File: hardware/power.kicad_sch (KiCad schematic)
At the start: 15 parts, among them J4 Conn_Coaxial_Small, J5 batt, Q1 PMOS, Q2 PMOS, SW41 SW_SPDT, U4 TLV62569DBV

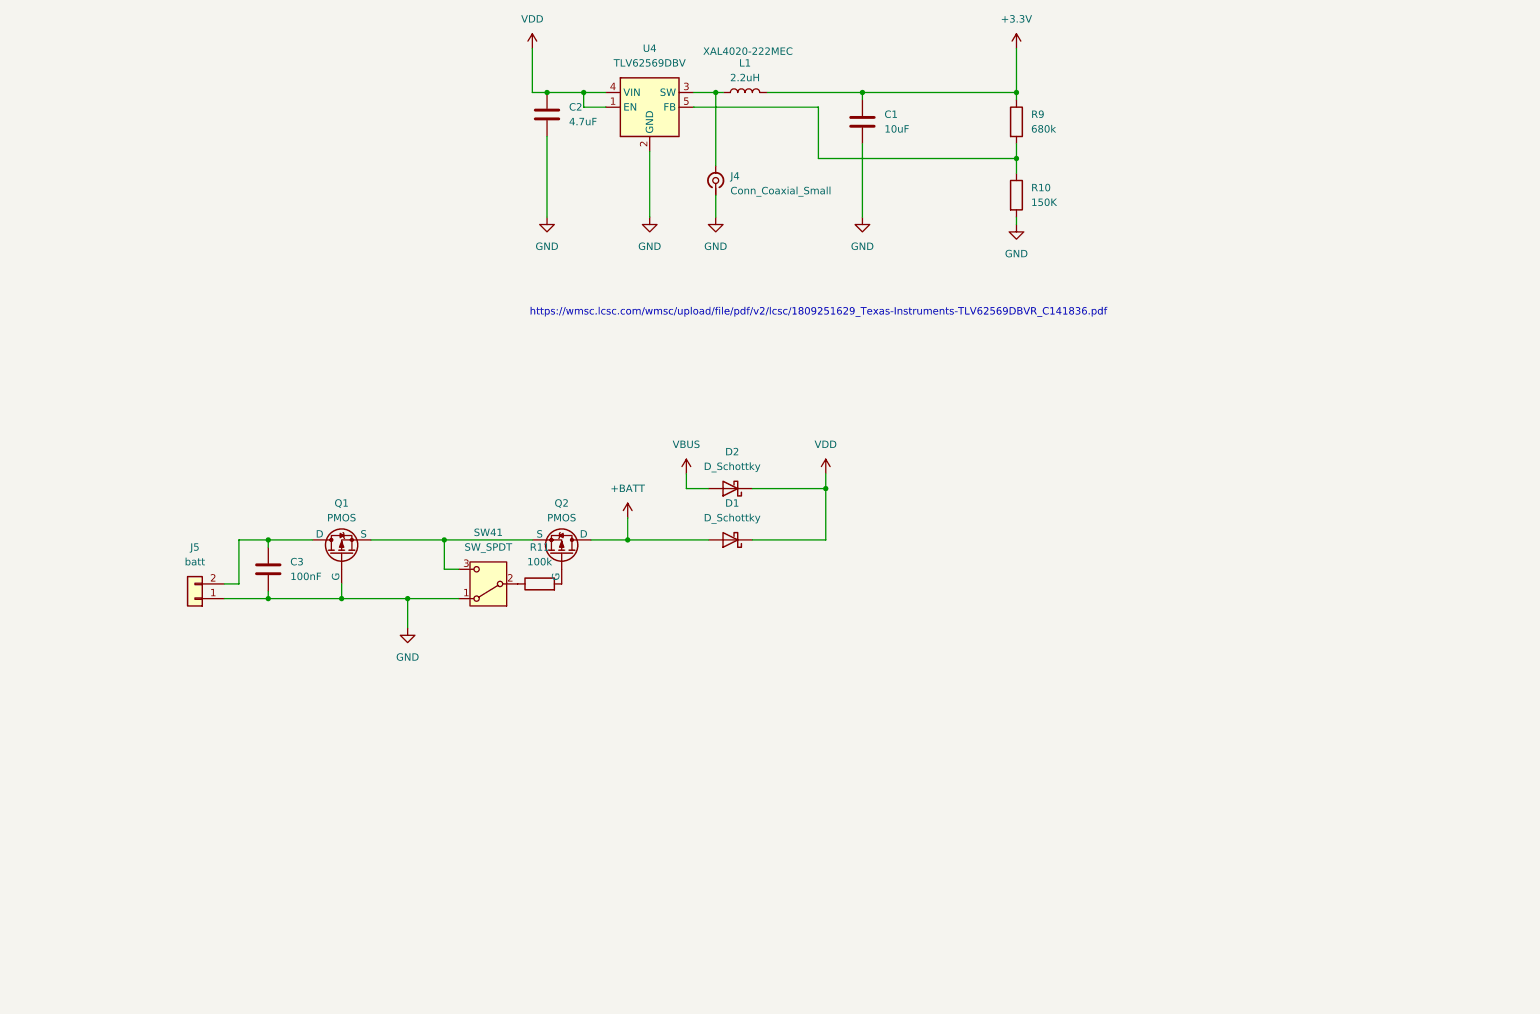
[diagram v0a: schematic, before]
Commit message: Add the battery charger
This commit will remove the old battery switching logic, and replace it
with a BQ24075.
Some more info are required, so the component that need a value are marked as TBD
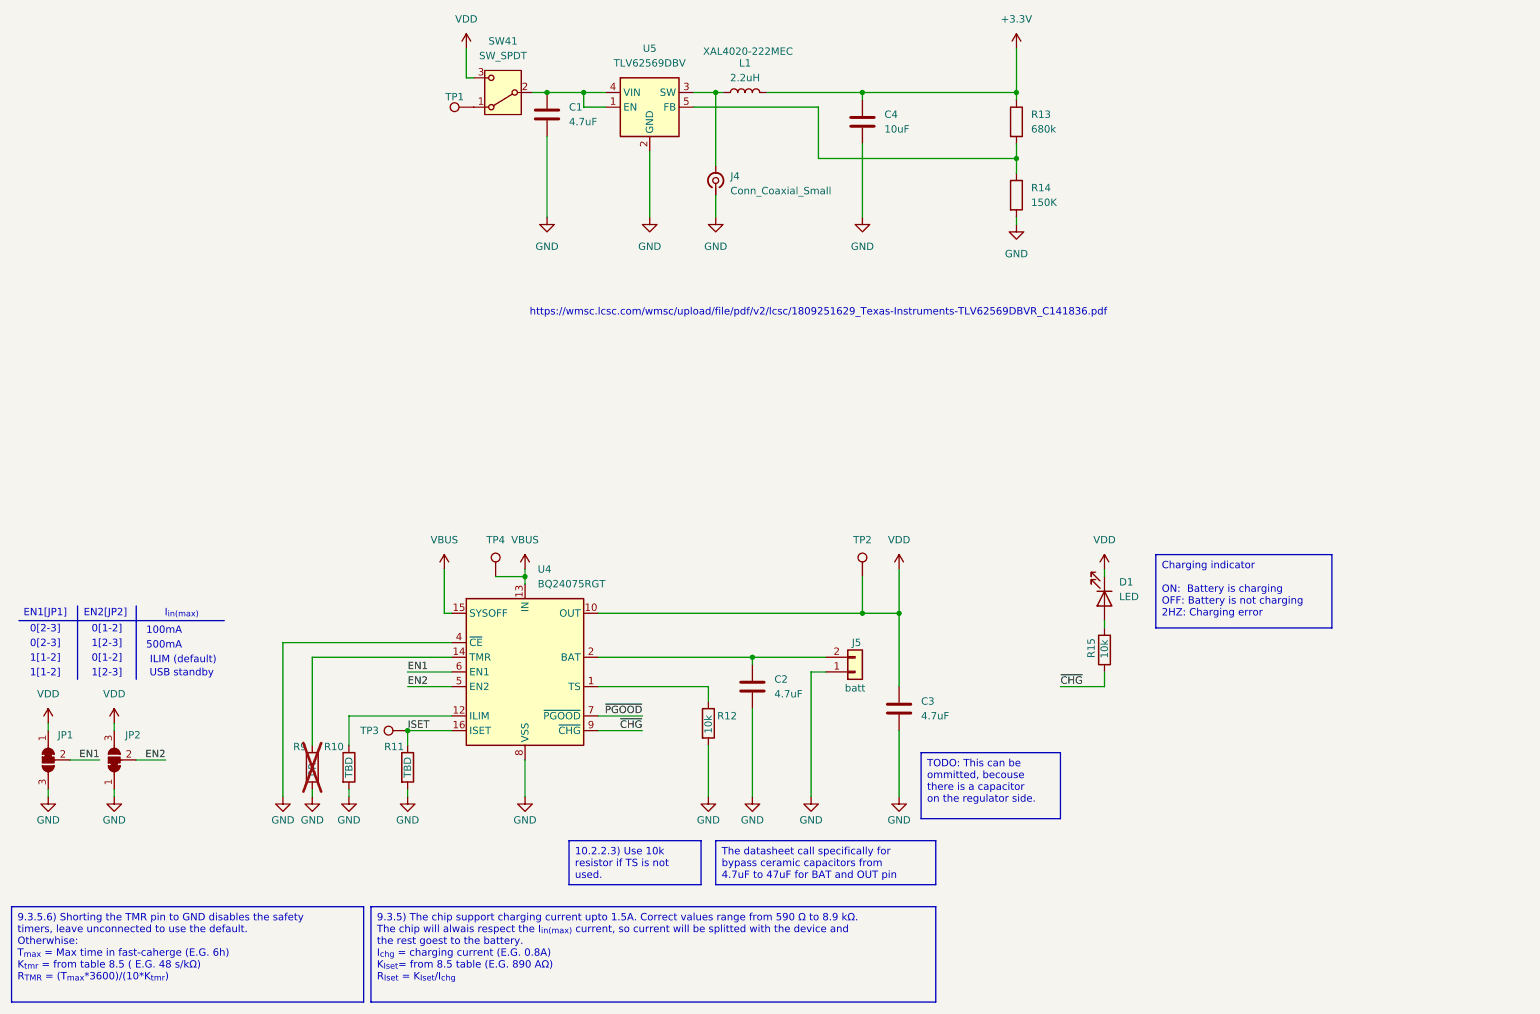
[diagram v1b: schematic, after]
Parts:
- removed D1, D2: D_Schottky, symbol Device:D_Schottky
- removed Q1, Q2: PMOS, symbol Simulation_SPICE:PMOS
- added C2: 4.7uF, symbol Device:C
- added D1: LED, symbol Device:LED
- added JP1, JP2: SolderJumper_3_Bridged12, Jumper:SolderJumper-3_P1.3mm_Bridged12_RoundedPad1.0x1.5mm, symbol Jumper:SolderJumper_3_Bridged12
- added R10: TBD, symbol Device:R
- added R12, R15: 10k, symbol Device:R
- added R9: 0R, symbol Device:R
- added TP1, TP2, TP3, TP4: TestPoint, TestPoint:TestPoint_Pad_D2.0mm, symbol Connector:TestPoint
- added U4: BQ24075RGT, Package_DFN_QFN:VQFN-16-1EP_3x3mm_P0.5mm_EP1.6x1.6mm, symbol Battery_Management:BQ24075RGT
- C3: value 100nF -> 4.7uF
- R11: value 100k -> TBD
- renumbered C2 to C1, C1 to C4, R9 to R13, R10 to R14, U4 to U5
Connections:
- net GND: now also R11.2, C2.2, JP1.3 (B), JP2.1 (A), R10.2, R12.2, R9.2, U4.17 (VSS), U4.4 (~{CE}), U4.8 (VSS); no longer SW41.1 (A)
- net VBUS: now also TP4.1, U4.13 (IN), U4.15 (SYSOFF)
- net VDD: now also C3.1, SW41.3 (C), D1.1 (K), JP1.1 (A), JP2.3 (B), TP2.1, U4.10 (OUT), U4.11 (OUT); no longer C1.1, U5.1 (EN), U5.4 (VIN)
- net at J5.2 (Pin_2): now also C2.1, U4.2 (BAT), U4.3 (BAT); no longer C3.1
- net at SW41.2 (B): now also C1.1, U5.1 (EN), U5.4 (VIN); no longer R11.1
- new net: SW41.1 (A), TP1.1
- new net: D1.2 (A), R15.2
- new net: R12.1, U4.1 (TS)
- new net: R10.1, U4.12 (ILIM)
- new net: R9.1, U4.14 (TMR)
- new net EN1: JP1.2 (C), U4.6 (EN1)
- new net EN2: JP2.2 (C), U4.5 (EN2)
- new net ISET: R11.1, TP3.1, U4.16 (ISET)
- new net ~{CHG}: R15.1, U4.9 (~{CHG})
- new net ~{PGOOD}: U4.7 (~{PGOOD})
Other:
- note added: "0[1-2]"
- note added: "0[2-3]"
- note added: "100mA"
- note added: "1[1-2]"
- note added: "1[2-3]"
- note added: "500mA"
- note added: "EN1[JP1]"
- note added: "EN2[JP2]"
- note added: "ILIM (default)"
- note added: "I_{in(max)}"
- note added: "USB standby"

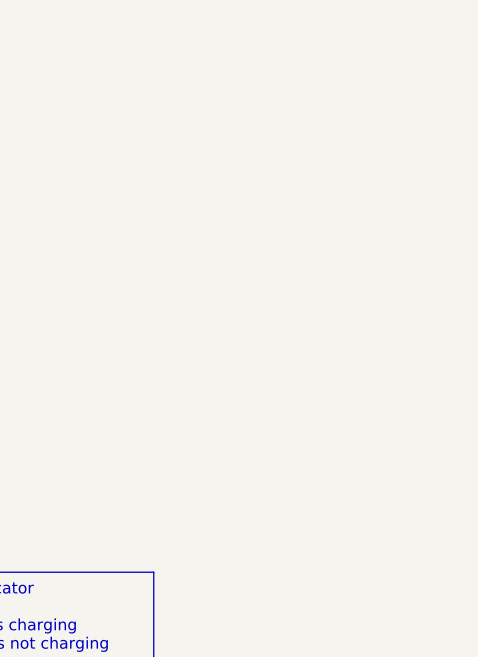
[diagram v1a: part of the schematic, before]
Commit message: chg pin
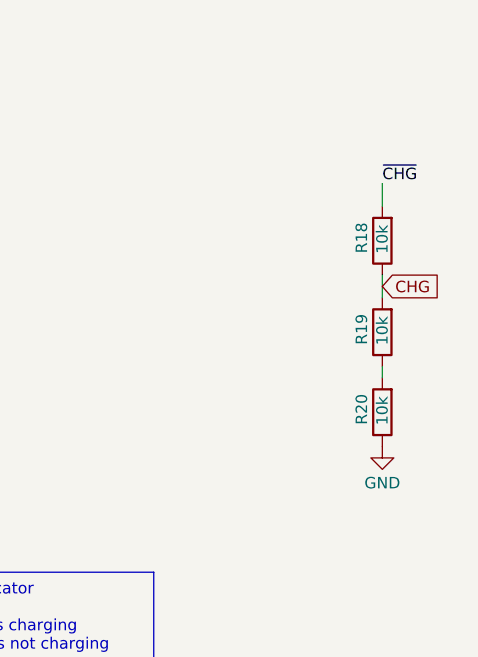
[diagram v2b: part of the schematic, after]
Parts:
- added R18, R19, R20: 10k, symbol Device:R
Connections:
- net GND: now also R20.1
- net ~{CHG}: now also R18.2
- new net: R19.1, R20.2
- new net CHG: R18.1, R19.2

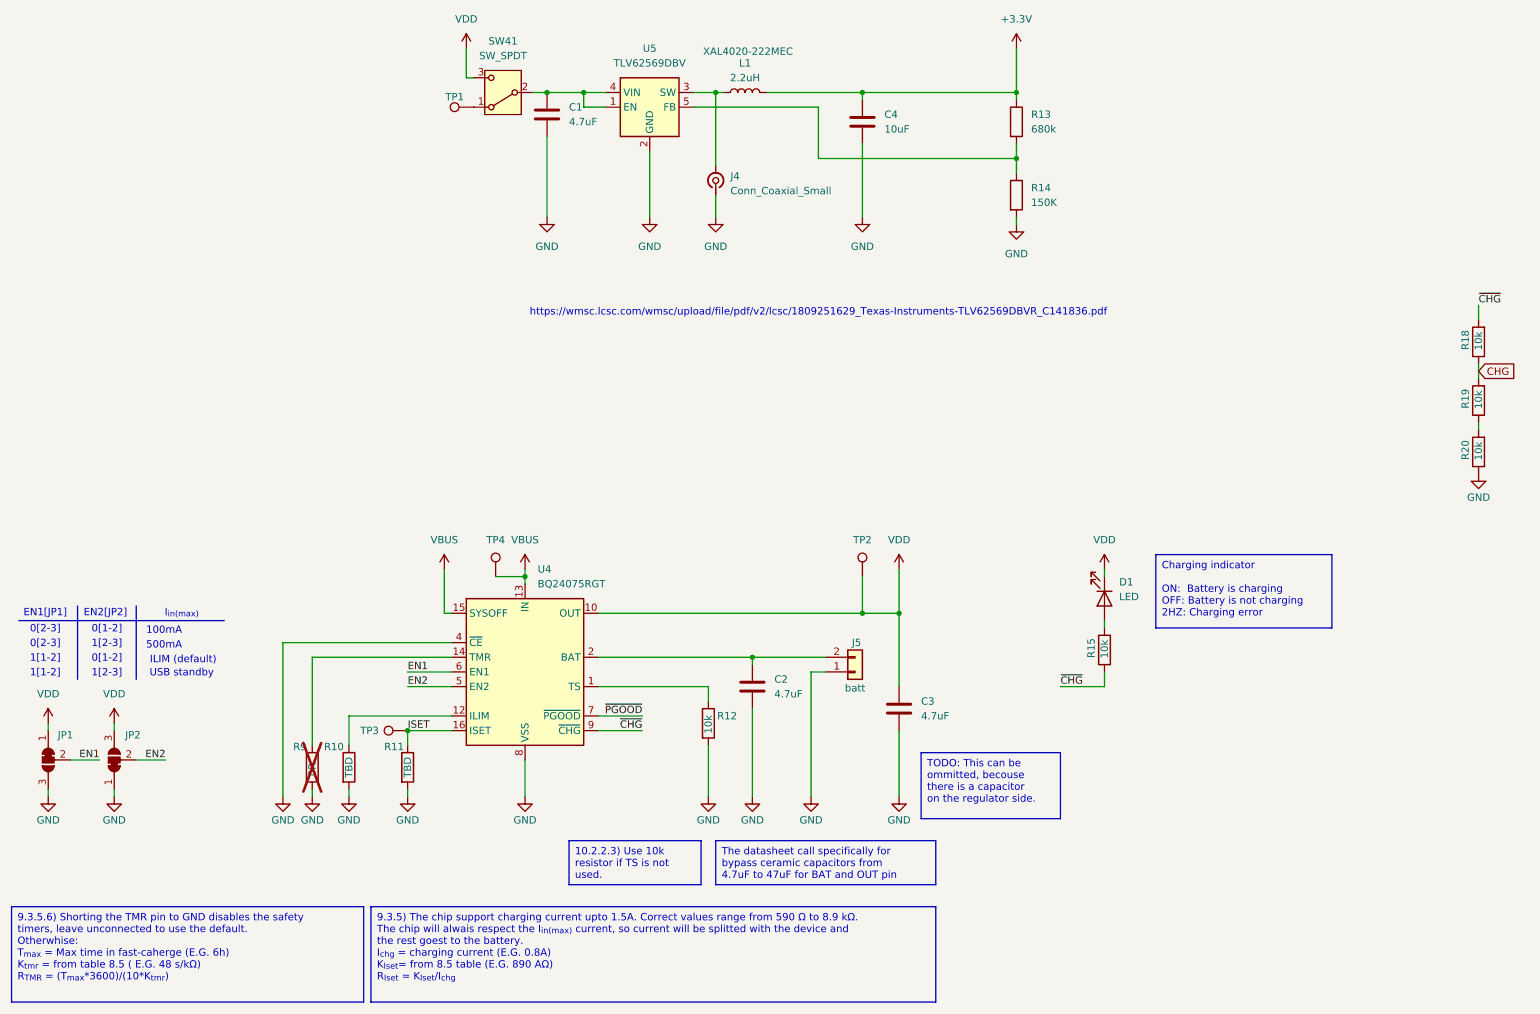
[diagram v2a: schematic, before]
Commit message: Make the badge power on on usb connected
Fix charge led polarity :D
Isolate more the CHG signal from the BQ24075
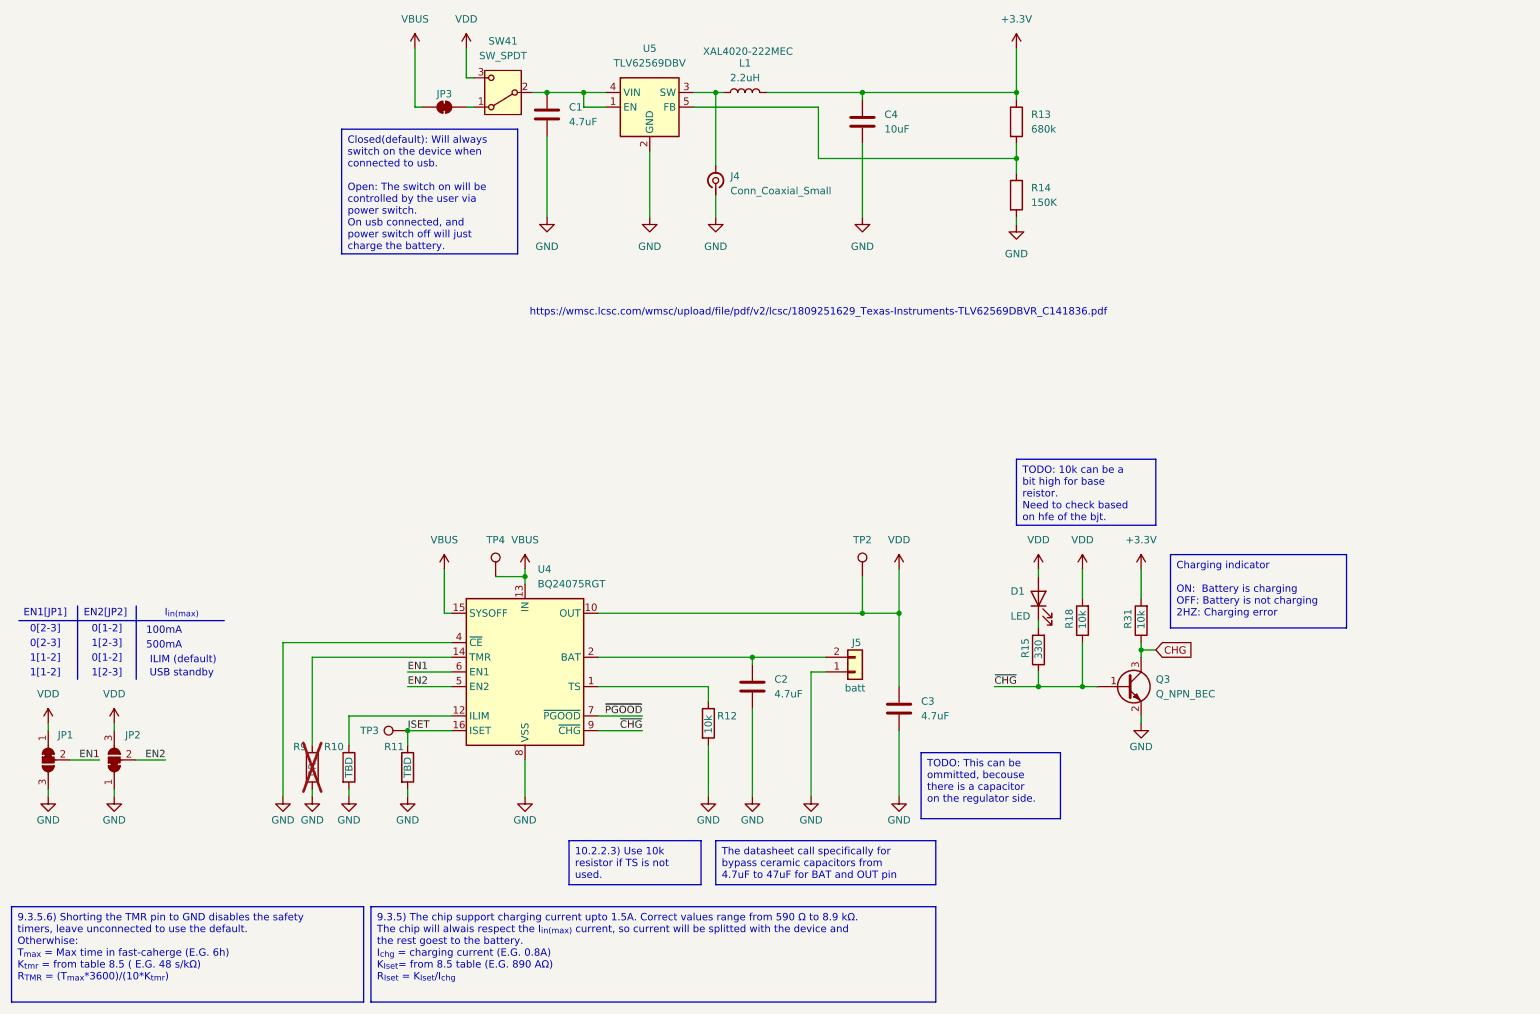
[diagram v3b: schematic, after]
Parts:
- removed R19, R20: 10k, symbol Device:R
- removed TP1: TestPoint, TestPoint:TestPoint_Pad_D2.0mm, symbol Connector:TestPoint
- added JP3: Grumpy wifasoi jumper, Jumper:SolderJumper-2_P1.3mm_Bridged_RoundedPad1.0x1.5mm, symbol Jumper:SolderJumper_2_Bridged
- added Q3: Q_NPN_BEC, symbol Device:Q_NPN_BEC
- added R31: 10k, symbol Device:R
- JP1: value SolderJumper_3_Bridged12 -> EN1
- JP2: value SolderJumper_3_Bridged12 -> EN2
- R15: value 10k -> 330
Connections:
- net +3.3V: now also R31.2
- net CHG: now also Q3.3 (C), R31.1; no longer R18.1
- net GND: now also Q3.2 (E)
- net VBUS: now also JP3.1 (A)
- net VDD: now also D1.2 (A), R18.2; no longer D1.1 (K)
- net ~{CHG}: now also R18.1, Q3.1 (B); no longer R18.2
- net at SW41.1 (A): now also JP3.2 (B)
- net at R15.2: now also D1.1 (K); no longer D1.2 (A)
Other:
- moved on the sheet: D1, R15

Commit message: rename power symbols, power switch on EN pin instead of VIN
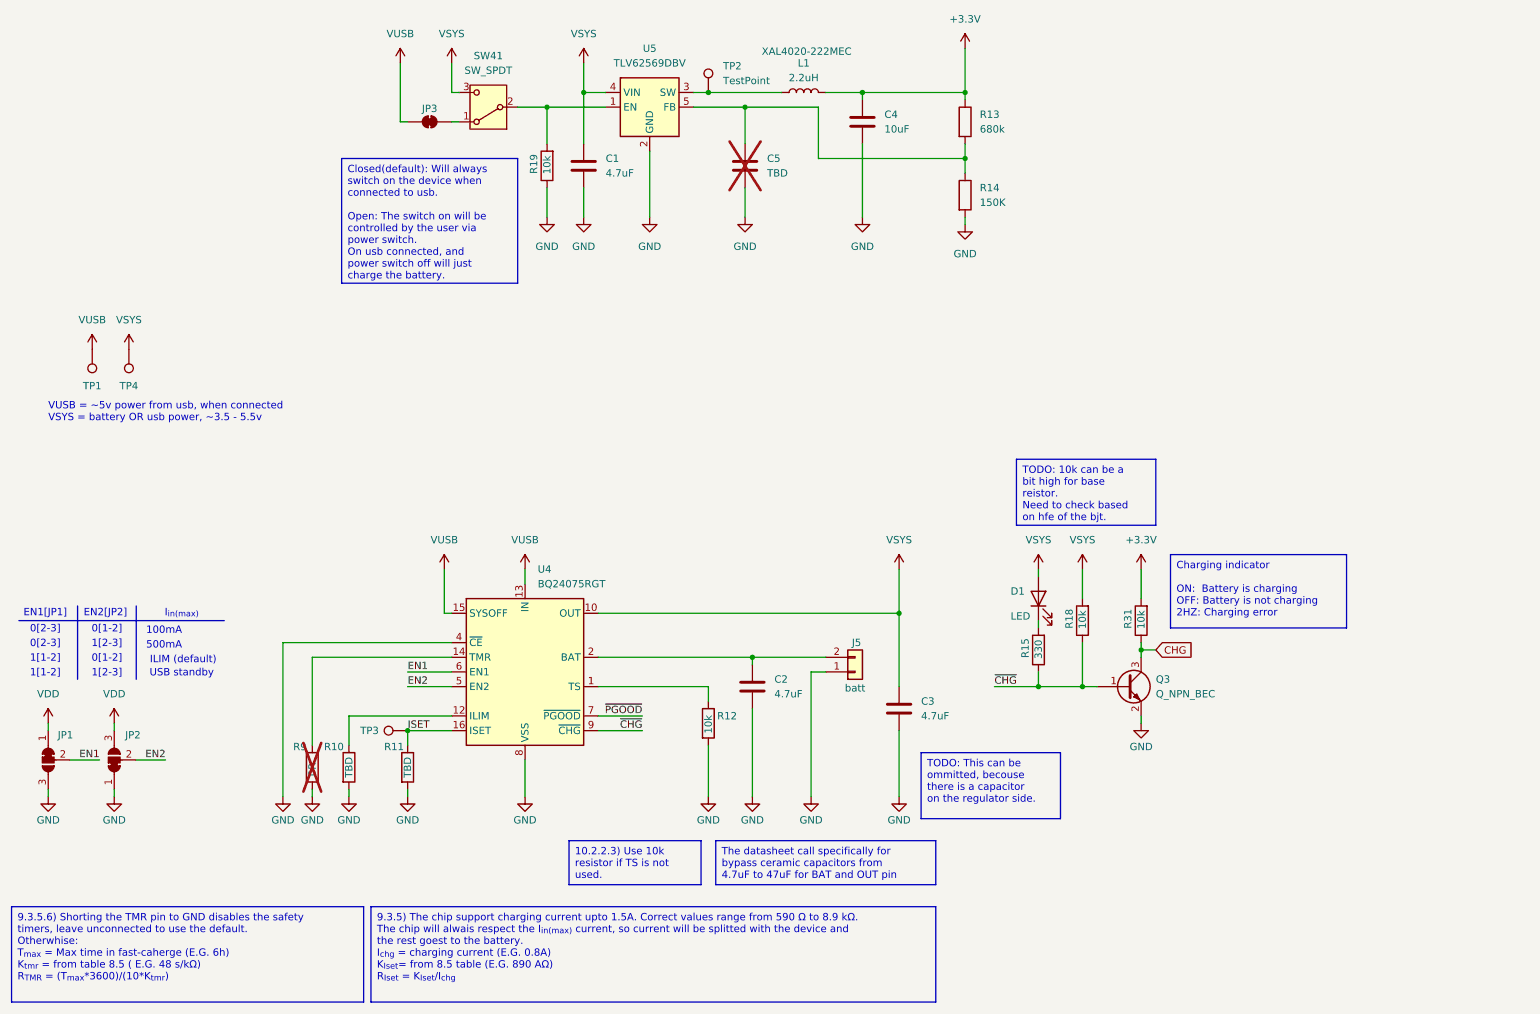
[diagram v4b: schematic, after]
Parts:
- removed J4: Conn_Coaxial_Small, symbol Connector:Conn_Coaxial_Small
- added C5: TBD, symbol Device:C
- added R19: 10k, symbol Device:R
- added TP1: TestPoint, TestPoint:TestPoint_Pad_D2.0mm, symbol Connector:TestPoint
- TP2: footprint TestPoint:TestPoint_Pad_D2.0mm -> (none)
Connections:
- net GND: now also C5.2, R19.1
- net VDD: no longer C3.1, D1.2 (A), R18.2, SW41.3 (C), TP2.1, U4.10 (OUT), U4.11 (OUT)
- net at SW41.2 (B), U5.1 (EN): now also R19.2; no longer C1.1, U5.4 (VIN)
- net at R13.2, R14.1, U5.5 (FB): now also C5.1
- net at L1.1, U5.3 (SW): now also TP2.1
- net VBUS renamed VUSB
- net VUSB: now also TP1.1; no longer TP4.1
- new net VSYS: C1.1, C3.1, D1.2 (A), R18.2, SW41.3 (C), TP4.1, U4.10 (OUT), U4.11 (OUT), U5.4 (VIN)
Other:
- note added: "VUSB = ~5v power from usb, when connected VSYS = battery OR usb power, ~3.5 - 5.5v"
- note removed: "https://wmsc.lcsc.com/wmsc/upload/file/pdf/v2/lcsc/1809251629_Texas-Instruments-TLV62569DBVR_C141836.pdf"
- moved on the sheet: C1, JP3, L1, R13, R14, SW41
